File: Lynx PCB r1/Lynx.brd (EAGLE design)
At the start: 124.3 x 51 mm, 105 parts, among them IC3 ICL7660, Q1 8MHz, X1 BU-SMA-V, X2 BU-SMA-V

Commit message: All routed
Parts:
- moved C33 32.5 mm to (98.5, 14.4)
- moved C30 22.9 mm to (95.0, 7.00), turned to 270 degrees
- moved C32 17.1 mm to (91.3, 7.00), turned to 270 degrees
- moved C31 16.7 mm to (84.1, 9.95), turned to 180 degrees
- moved C24 6.46 mm to (76.3, 23.2), turned to 270 degrees
- moved C26 5.47 mm to (75.8, 42.0), turned to 270 degrees
- moved C27 4.41 mm to (75.8, 45.0), turned to 90 degrees
- moved C14 3.10 mm to (110.3, 16.0), turned to 180 degrees
- moved C9 2.10 mm to (78.3, 23.2)
- moved R7 2.10 mm to (99.1, 16.4)
- moved C11 1.95 mm to (77.8, 42.0)
- moved C15 1.90 mm to (110.3, 6.30), turned to 180 degrees
- moved R3 1.90 mm to (76.8, 20.1), turned to 0 degrees
- moved R6 1.59 mm to (76.8, 38.9), turned to 180 degrees
- moved C25 0.46 mm to (76.3, 26.2), turned to 90 degrees
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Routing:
- net +3V3: track 420.9 -> 493.6 mm, vias 17 -> 20
- net GND: track 706.1 -> 743.0 mm
- net SPI2-CS: track 66.0 -> 86.1 mm
- net SPI2-SCK: track 65.6 -> 84.6 mm
- net +5V: track 76.6 -> 73.2 mm
- net N$24: track 2.79 -> 5.79 mm
- net N$14: track 49.6 -> 52.6 mm
- net N$25: track 2.52 -> 5.17 mm
- net N$29: track 35.2 -> 37.7 mm
- net N$10: track 2.05 -> 4.15 mm
- net BBPI: vias 2 -> 0

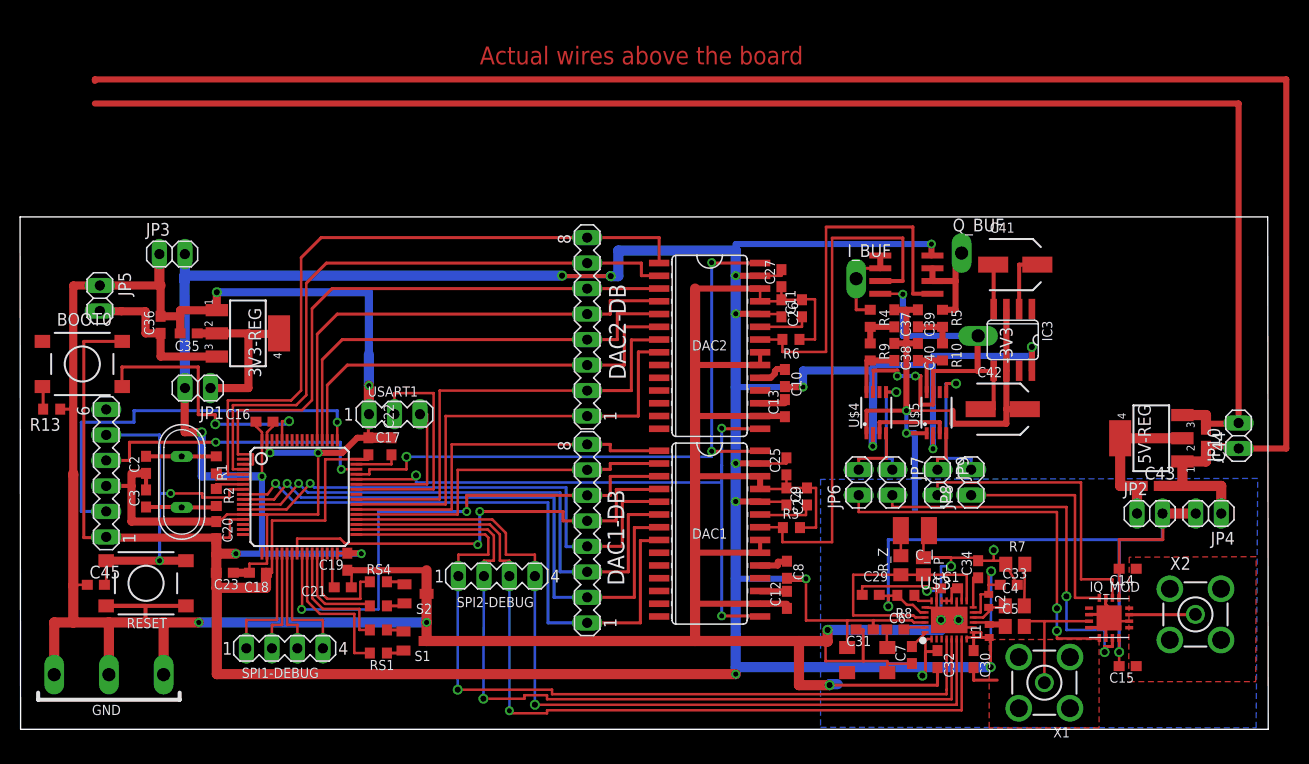
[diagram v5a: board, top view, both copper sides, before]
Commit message: Added 0.54v reference souce, made DRC happy
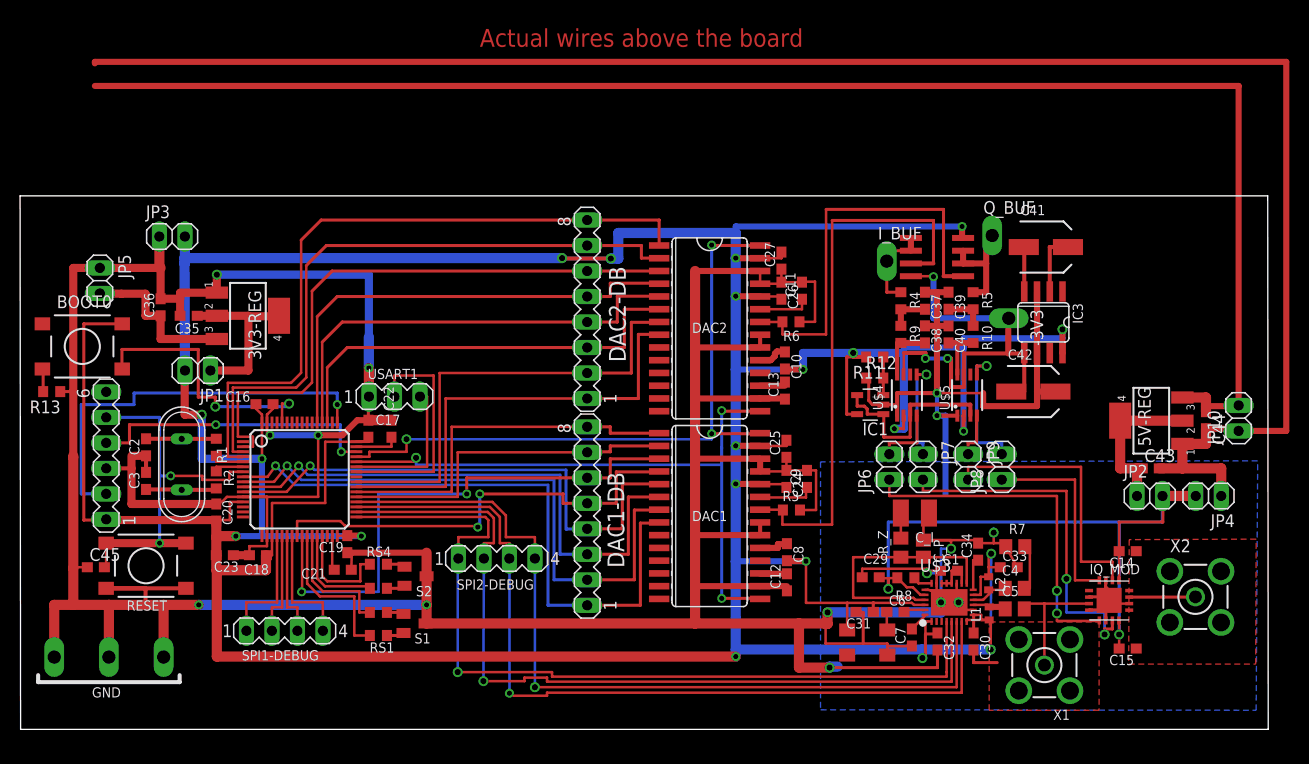
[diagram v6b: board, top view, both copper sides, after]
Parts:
- added IC1: LM321MF, linear:SOT23-5
- added R11: 50k, resistor:R0603
- added R12: 10k, resistor:R0603
- moved C41 3.52 mm to (102.2, 48.0)
- moved C42 3.52 mm to (100.9, 33.6)
- moved IC3 3.52 mm to (101.9, 40.5)
- moved R10 3.52 mm to (94.9, 39.4)
- moved R5 3.52 mm to (94.9, 42.7)
- moved -3V3 3.52 mm to (98.5, 41.0)
- moved C37 3.52 mm to (90.1, 42.7)
- moved C38 3.52 mm to (90.1, 39.4)
- moved C39 3.52 mm to (92.5, 42.7)
- moved C40 3.52 mm to (92.5, 39.4)
- moved IC2 3.52 mm to (91.3, 47.0)
- moved I_BUF 3.52 mm to (86.3, 46.6)
- moved Q_BUF 3.52 mm to (96.8, 49.2)
- moved R4 3.52 mm to (87.7, 42.7)
- moved R9 3.52 mm to (87.7, 39.4)
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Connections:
- new net N$42: IC1.3, R11.1, R12.2
- net +0.54V: now also IC1.1, IC1.4
- net +3V3: now also IC1.5, R11.2
- net GND: now also IC1.2, R12.1
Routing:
- net +3V3: track 493.6 -> 512.3 mm, vias 20 -> 21
- net +0.54V: track 8.20 -> 19.7 mm
- net GND: track 743.0 -> 748.8 mm
- net N$42: track 0.00 -> 3.81 mm
- net BBPI: track 30.2 -> 26.9 mm
- net BBPQ: track 39.5 -> 36.3 mm
- net BBMQ: track 38.3 -> 35.1 mm
- net BBMI: track 23.0 -> 19.8 mm
- net N$29: track 37.7 -> 40.8 mm
- net N$14: track 52.6 -> 55.7 mm
- net N$10: track 4.15 -> 5.20 mm
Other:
- board size 124.3 x 51 mm -> 124.3 x 53.1 mm

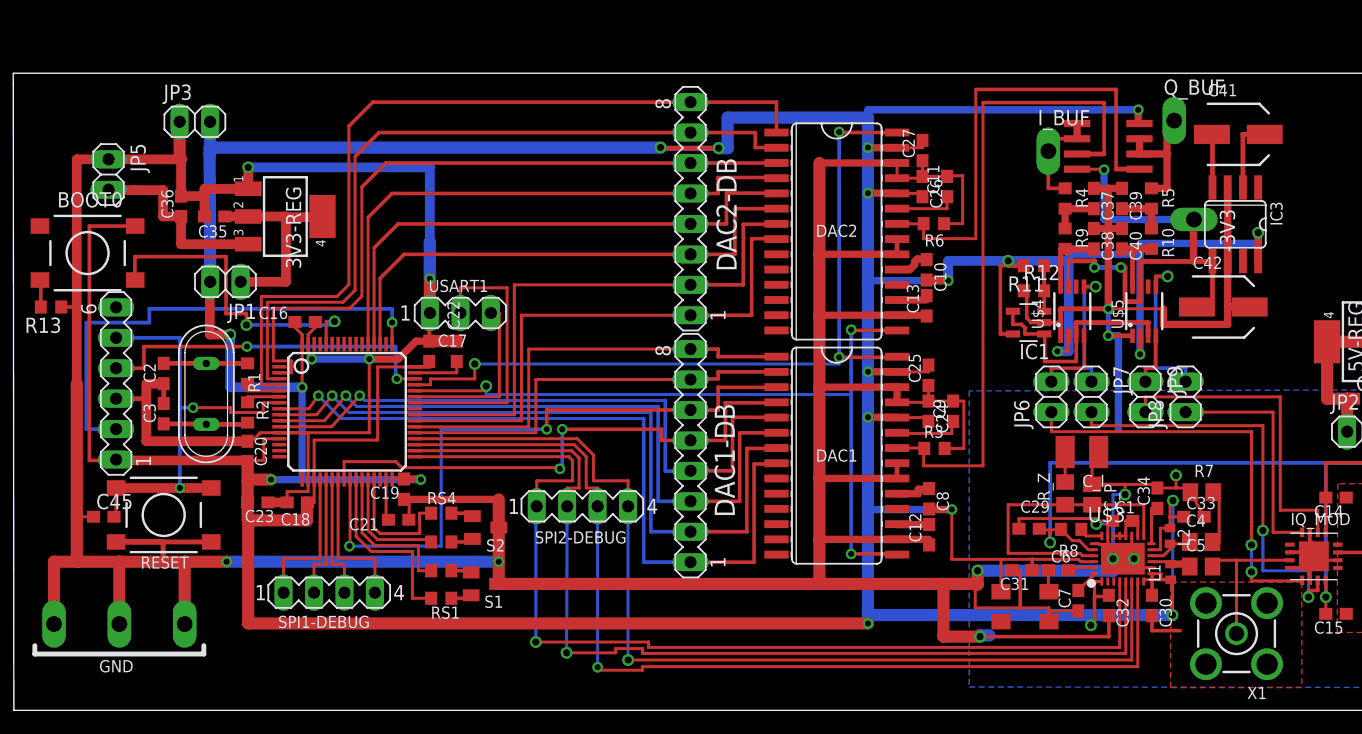
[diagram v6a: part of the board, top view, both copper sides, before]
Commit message: Description text, pll-stat line
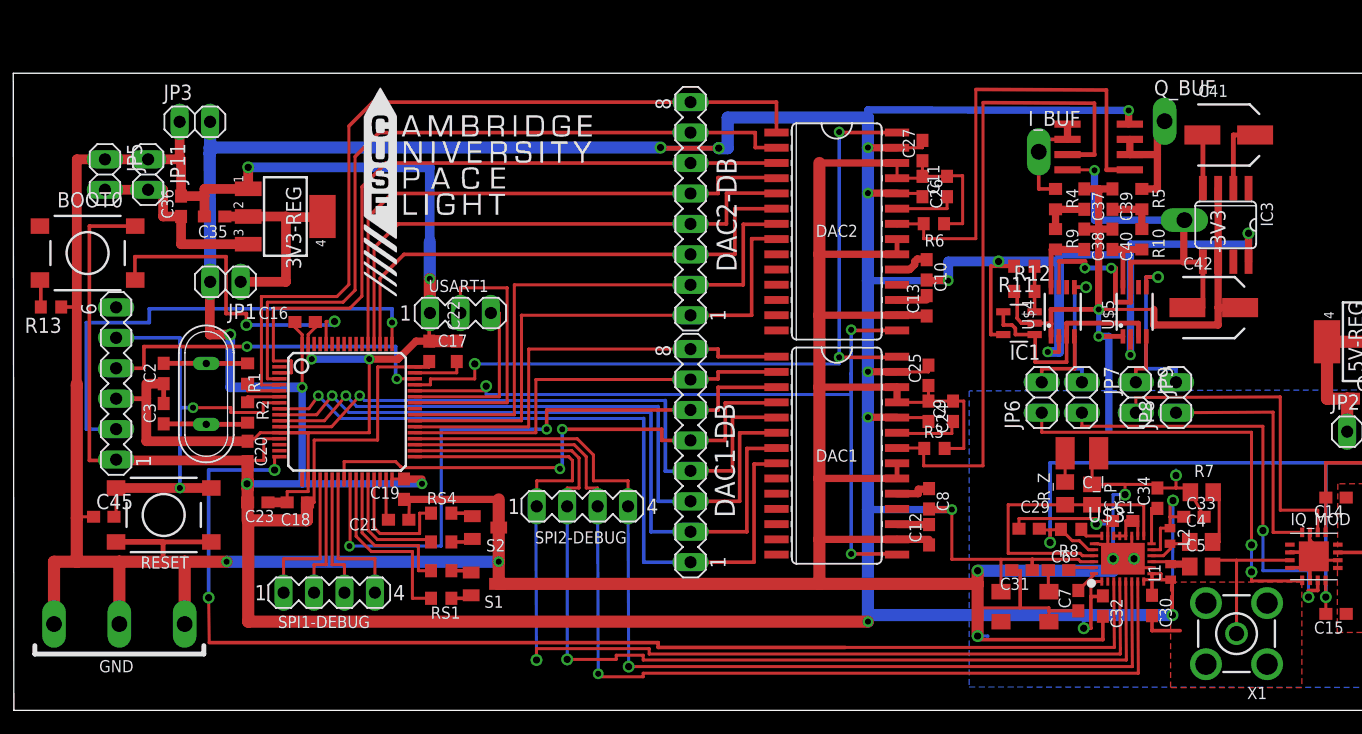
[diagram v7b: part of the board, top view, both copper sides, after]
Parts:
- added JP11: Power In, pinhead:1X02
- added U$2: (no value), Lynx components:CUSF_LOGO_LARGE
- moved IC1 0.80 mm to (83.8, 32.3)
- moved R10 0.80 mm to (94.1, 39.3)
- moved R5 0.80 mm to (94.1, 42.6)
- moved C41 0.80 mm to (101.3, 48.0)
- moved C42 0.80 mm to (100.1, 33.6)
- moved IC3 0.80 mm to (101.1, 40.5)
- moved JP7 0.80 mm to (89.1, 26.1)
- moved JP9 0.80 mm to (93.6, 26.1)
- moved -3V3 0.80 mm to (97.7, 40.9)
- moved C37 0.80 mm to (89.3, 42.6)
- moved C38 0.80 mm to (89.3, 39.3)
- moved C39 0.80 mm to (91.7, 42.6)
- moved C40 0.80 mm to (91.7, 39.3)
- moved Q_BUF 0.80 mm to (96.0, 49.1)
- moved R11 0.80 mm to (84.3, 37.0)
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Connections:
- removed net PLL_STAT: U$3.3
- new net PLL-STAT: U$1.16, U$3.3
- net GND: now also JP11.1
- net POWER-IN: now also JP11.2
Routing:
- net PLL-STAT: track 0.00 -> 102.8 mm, vias 0 -> 2
- net SPI2-CS: track 86.1 -> 89.1 mm
- net GND: track 748.8 -> 745.9 mm
- net +3V3: track 512.3 -> 513.5 mm
- net SPI2-MOSI: track 84.0 -> 85.1 mm
- net SPI2-MISO: track 85.9 -> 87.0 mm
- net SPI2-SCK: track 84.6 -> 85.7 mm
- net BBMI: track 19.8 -> 20.6 mm
- net BBPI: track 26.9 -> 27.7 mm
- net N$29: track 40.8 -> 40.0 mm
- net N$14: track 55.7 -> 54.9 mm
- net BBPQ: track 36.3 -> 37.0 mm
- net BBMQ: track 35.1 -> 35.8 mm
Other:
- board text added: "Developement Board"
- board text added: "Joe Roberts"
- board text added: "Lynx Experimental Radio"
- board text added: "r1"

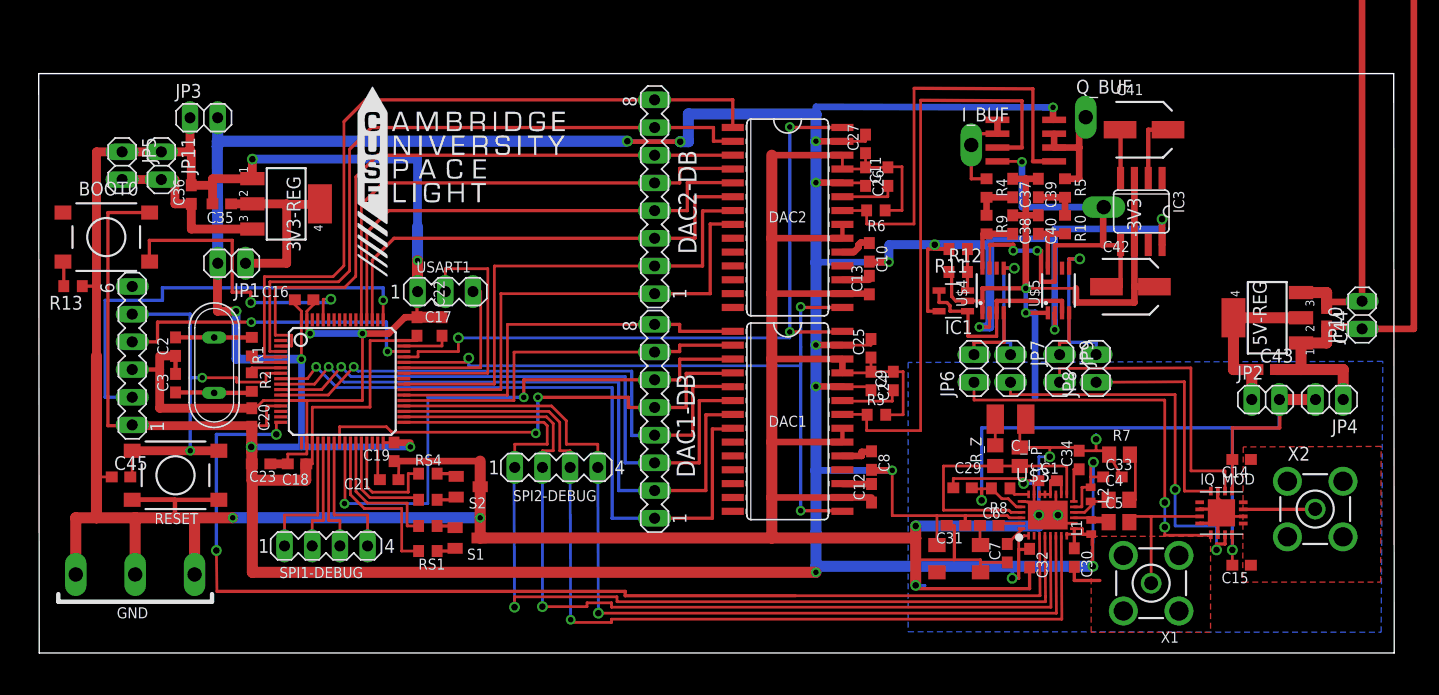
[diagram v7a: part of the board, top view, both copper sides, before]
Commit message: started sorting out the silkscreen
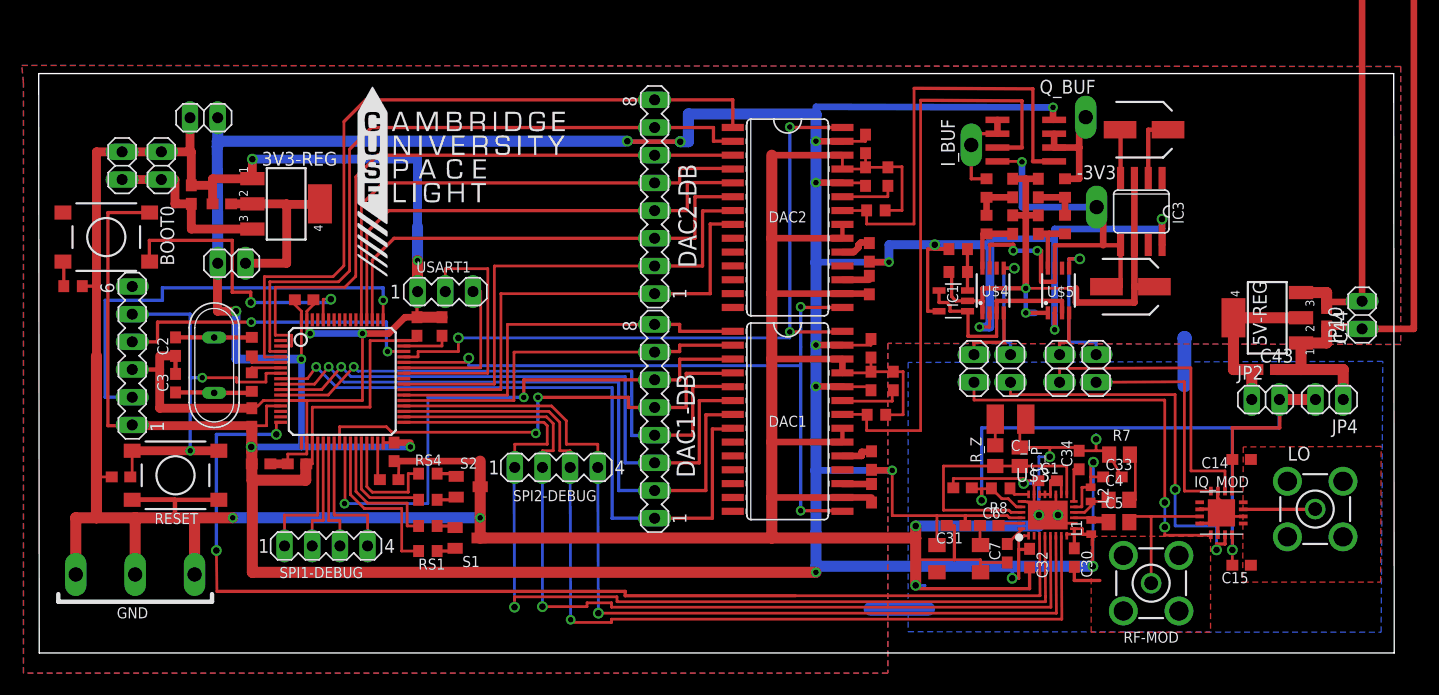
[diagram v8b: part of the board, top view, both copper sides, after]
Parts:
- R13: value 1500 -> 1k5
- moved -3V3 0.65 mm to (97.0, 40.9), turned to 0 degrees
- renumbered X1 to RF-MOD, X2 to LO
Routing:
- net GND: track 745.9 -> 747.8 mm
